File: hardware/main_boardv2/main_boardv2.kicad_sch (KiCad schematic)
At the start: 4 parts

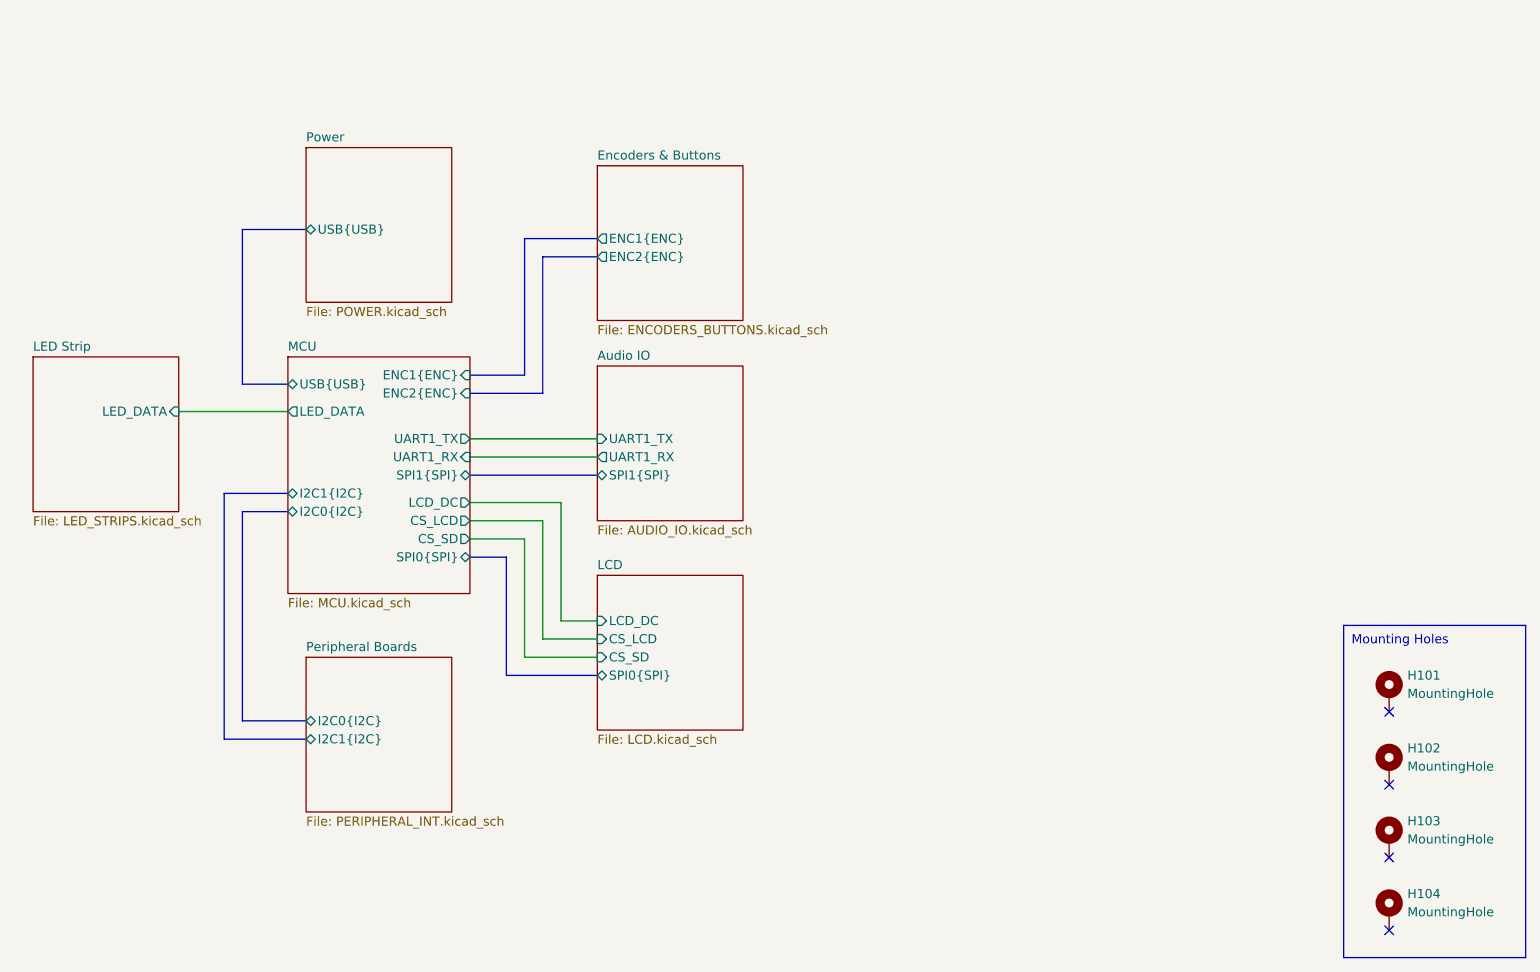
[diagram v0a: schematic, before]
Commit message: dubious hardware schematic 'done'. need to go back and revise passives and verify IC connections, esp the DAC. modified readme
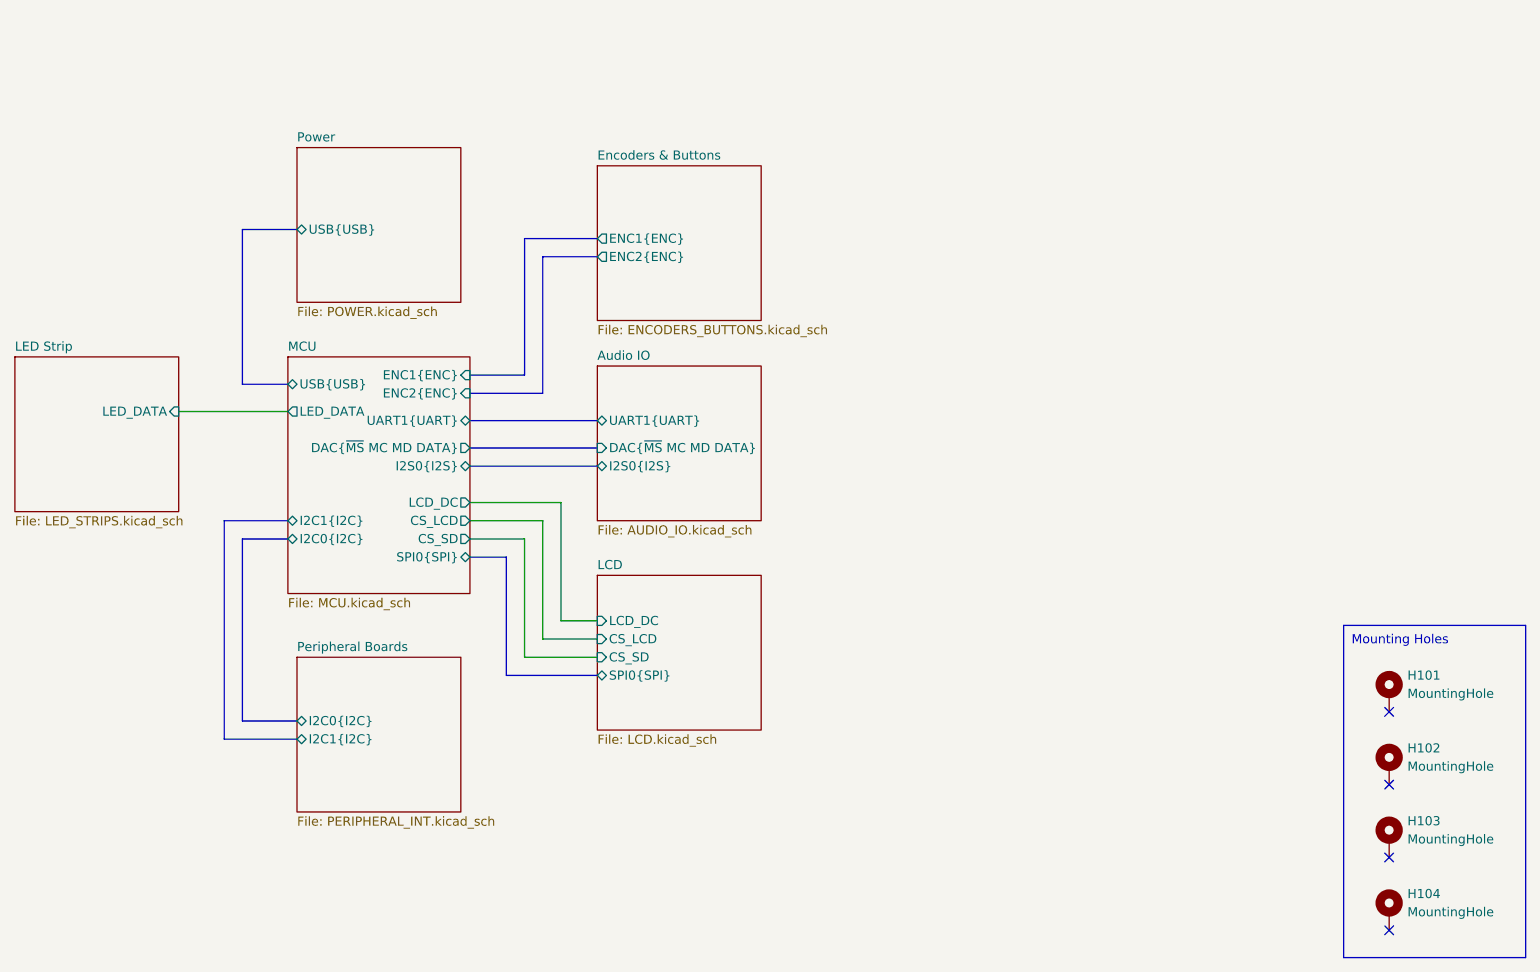
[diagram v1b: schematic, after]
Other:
- sheet Audio IO ports: added DAC{~{MS} MC MD DATA}, I2S0{I2S}, UART1{UART}; removed SPI1{SPI}, UART1_RX, UART1_TX
- sheet MCU ports: added DAC{~{MS} MC MD DATA}, I2S0{I2S}, UART1{UART}; removed SPI1{SPI}, UART1_RX, UART1_TX

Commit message: schematic sorta done? resized all RC packages to 0805
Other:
- sheet LCD ports: added DC_LCD; removed LCD_DC
- sheet MCU ports: added DC_LCD, S[0..3]; removed I2C1{I2C}, LCD_DC
- sheet Peripheral Boards ports: added S[0..3]; removed I2C1{I2C}
- note added: "TODO: remap logic analyzer things"
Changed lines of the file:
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@@
+		)
+	)
+	(text "TODO: remap logic analyzer things"
+		(exclude_from_sim no)
+		(at 119.126 33.02 0)
+		(effects
+			(font
+				(size 3 3)
+			)
 		)
 	)
@@
 			)
 		)
-		(pin "LCD_DC" output
+		(pin "DC_LCD" output
 			(at 133.35 97.79 0)
 			(effects
@@
 			)
 		)
-		(pin "I2C1{I2C}" bidirectional
+		(pin "S[0..3]" output
 			(at 107.95 100.33 180)
 			(effects
@@
 			)
 		)
-		(pin "I2C1{I2C}" bidirectional
+		(pin "S[0..3]" input
 			(at 109.22 130.81 180)
 			(effects
@@
 			)
 		)
-		(pin "LCD_DC" input
+		(pin "DC_LCD" input
 			(at 151.13 114.3 180)
 			(effects
